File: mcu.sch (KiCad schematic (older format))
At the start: 22 parts, among them U201 STM32F072C8Tx, Y201 8MHz

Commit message: Add Fit, Manufacturer, MPN fields
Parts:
- C201, C202, R203, Y201: Fit (none) -> fit: none
- C203, C204, C205, C206, C207, C208, R201, R202, R204, W201, W202, W203, W204, W205, W206, W207, W208: Fit (none) -> fit:
- U201: Fit (none) -> fit:; MPN (none) -> STM32F072C8T6; Manufacturer (none) -> ST
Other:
- note added: "Short this footprint and power up the board to enter DFU bootloader mode."
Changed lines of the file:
@@
 F 2 "Housings_QFP:LQFP-48_7x7mm_Pitch0.5mm" H 9500 5675 50  0000 R TNN
 F 3 "" H 5800 3900 50  0000 C CNN
+F 4 "STM32F072C8T6" H 5800 3900 50  0001 C CNN "MPN"
+F 5 "ST" H 5800 3900 50  0001 C CNN "Manufacturer"
+F 6 "fit: " H 5800 3900 50  0001 C CNN "Fit"
 	1    5800 3900
 	1    0    0    -1
@@
 U 1 1 56F47B56
 P 1350 3150
-F 0 "Y201" H 1350 3250 50  0000 C CNN
-F 1 "8MHz" H 1350 3050 50  0000 C CNN
+F 0 "Y201" V 1278 3238 50  0000 L CNN
+F 1 "8MHz" V 1369 3238 50  0000 L CNN
 F 2 "Crystals:ABM3" H 1350 3150 50  0001 C CNN
 F 3 "" H 1350 3150 50  0000 C CNN
+F 4 "fit: none" V 1441 3238 25  0000 L CNN "Fit"
 	1    1350 3150
 	0    1    1    0
@@
 F 2 "Measurement_Points:Measurement_Point_Round-SMD-Pad_Small" H 9800 4700 50  0001 C CNN
 F 3 "" H 9800 4700 50  0000 C CNN
+F 4 "fit: " H 9600 4700 50  0001 C CNN "Fit"
 	1    9600 4700
 	0    1    1    0
@@
 F 2 "Measurement_Points:Measurement_Point_Round-SMD-Pad_Small" H 9800 4800 50  0001 C CNN
 F 3 "" H 9800 4800 50  0000 C CNN
+F 4 "fit: " H 9600 4800 50  0001 C CNN "Fit"
 	1    9600 4800
 	0    1    1    0
@@
 F 2 "Resistors_SMD:R_0603" V 1080 4400 50  0001 C CNN
 F 3 "" H 1150 4400 50  0000 C CNN
+F 4 "fit: " H 1150 4400 50  0001 C CNN "Fit"
 	1    1150 4400
 	0    -1   -1   0
@@
 F 2 "Resistors_SMD:R_0603" V 1080 4500 50  0001 C CNN
 F 3 "" H 1150 4500 50  0000 C CNN
+F 4 "fit: " H 1150 4500 50  0001 C CNN "Fit"
 	1    1150 4500
 	0    1    1    0
@@
 U 1 1 56F50DA3
 P 3900 6500
-F 0 "R203" V 3980 6500 50  0000 C CNN
-F 1 "R" V 3900 6500 50  0000 C CNN
+F 0 "R203" H 3970 6572 50  0000 L CNN
+F 1 "R" H 3970 6481 50  0000 L CNN
 F 2 "Resistors_SMD:R_0805" V 3830 6500 50  0001 C CNN
 F 3 "" H 3900 6500 50  0000 C CNN
+F 4 "fit: none" H 3970 6409 25  0000 L CNN "Fit"
 	1    3900 6500
 	1    0    0    -1
@@
 F 2 "Resistors_SMD:R_0603" V 3830 6900 50  0001 C CNN
 F 3 "" H 3900 6900 50  0000 C CNN
+F 4 "fit: " H 3900 6900 50  0001 C CNN "Fit"
 	1    3900 6900
 	-1   0    0    1
@@
 U 1 1 56F51A5F
 P 1100 3250
-F 0 "C202" V 950 3150 50  0000 L CNN
-F 1 "20pF" V 850 3150 50  0000 L CNN
+F 0 "C202" V 963 3250 50  0000 C CNN
+F 1 "20pF" V 872 3250 50  0000 C CNN
 F 2 "Capacitors_SMD:C_0603" H 1100 3250 50  0001 C CNN
 F 3 "" H 1100 3250 50  0000 C CNN
+F 4 "fit: none" V 800 3250 25  0000 C CNN "Fit"
 	1    1100 3250
 	0    -1   -1   0
@@
 F 2 "Capacitors_SMD:C_0603" H 2500 6850 50  0001 C CNN
 F 3 "" H 2500 6850 50  0000 C CNN
+F 4 "fit: " H 2500 6850 50  0001 C CNN "Fit"
 	1    2500 6850
 	1    0    0    -1
@@
 F 2 "Capacitors_SMD:C_0603" H 2200 6850 50  0001 C CNN
 F 3 "" H 2200 6850 50  0000 C CNN
+F 4 "fit: " H 2200 6850 50  0001 C CNN "Fit"
 	1    2200 6850
 	1    0    0    -1
@@
 F 2 "Capacitors_SMD:C_0603" H 1900 6850 50  0001 C CNN
 F 3 "" H 1900 6850 50  0000 C CNN
+F 4 "fit: " H 1900 6850 50  0001 C CNN "Fit"
 	1    1900 6850
 	1    0    0    -1
@@
 F 2 "Capacitors_SMD:C_0603" H 1600 6850 50  0001 C CNN
 F 3 "" H 1600 6850 50  0000 C CNN
+F 4 "fit: " H 1600 6850 50  0001 C CNN "Fit"
 	1    1600 6850
 	1    0    0    -1
@@
 F 2 "Capacitors_SMD:C_0805" H 2950 6850 50  0001 C CNN
 F 3 "" H 2950 6850 50  0000 C CNN
+F 4 "fit: " H 2950 6850 50  0001 C CNN "Fit"
 	1    2950 6850
 	1    0    0    -1
@@
 F 2 "Measurement_Points:Measurement_Point_Round-SMD-Pad_Small" H 1600 4400 50  0001 C CNN
 F 3 "" H 1600 4400 50  0000 C CNN
+F 4 "fit: " H 1400 4400 50  0001 C CNN "Fit"
 	1    1400 4400
 	1    0    0    -1
@@
 F 2 "Measurement_Points:Measurement_Point_Round-SMD-Pad_Small" H 1600 4500 50  0001 C CNN
 F 3 "" H 1600 4500 50  0000 C CNN
+F 4 "fit: " H 1400 4500 50  0001 C CNN "Fit"
 	1    1400 4500
 	-1   0    0    1
@@
 F 2 "Capacitors_SMD:C_0603" H 1350 2650 50  0001 C CNN
 F 3 "" H 1350 2650 50  0000 C CNN
+F 4 "fit: " H 1350 2650 50  0001 C CNN "Fit"
 	1    1350 2650
 	1    0    0    -1
@@
 F 2 "Measurement_Points:Measurement_Point_Round-SMD-Pad_Small" H 2200 5000 50  0001 C CNN
 F 3 "" H 2200 5000 50  0000 C CNN
+F 4 "fit: " H 2000 5000 50  0001 C CNN "Fit"
 	1    2000 5000
 	0    -1   -1   0
@@
 F 2 "Measurement_Points:Measurement_Point_Round-SMD-Pad_Small" H 2200 5100 50  0001 C CNN
 F 3 "" H 2200 5100 50  0000 C CNN
+F 4 "fit: " H 2000 5100 50  0001 C CNN "Fit"
 	1    2000 5100
 	0    -1   -1   0
@@
 F 2 "Measurement_Points:Measurement_Point_Round-SMD-Pad_Small" H 2200 5200 50  0001 C CNN
 F 3 "" H 2200 5200 50  0000 C CNN
+F 4 "fit: " H 2000 5200 50  0001 C CNN "Fit"
 	1    2000 5200
 	0    -1   -1   0
@@
 F 2 "Measurement_Points:Measurement_Point_Round-SMD-Pad_Small" H 2200 5300 50  0001 C CNN
 F 3 "" H 2200 5300 50  0000 C CNN
+F 4 "fit: " H 2000 5300 50  0001 C CNN "Fit"
 	1    2000 5300
 	0    -1   -1   0
@@
 U 1 1 56F518F0
 P 1100 3050
-F 0 "C201" V 1350 2950 50  0000 L CNN
-F 1 "20pF" V 1250 2950 50  0000 L CNN
+F 0 "C201" V 1381 3050 50  0000 C CNN
+F 1 "20pF" V 1290 3050 50  0000 C CNN
 F 2 "Capacitors_SMD:C_0603" H 1100 3050 50  0001 C CNN
 F 3 "" H 1100 3050 50  0000 C CNN
+F 4 "fit: none" V 1218 3050 25  0000 C CNN "Fit"
 	1    1100 3050
 	0    -1   -1   0
@@
 	900  3250 1000 3250
 Connection ~ 900  3150
+Text Notes 4250 6525 0    60   ~ 0
+Short this footprint and power up the board to enter DFU bootloader mode.
 $EndSCHEMATC

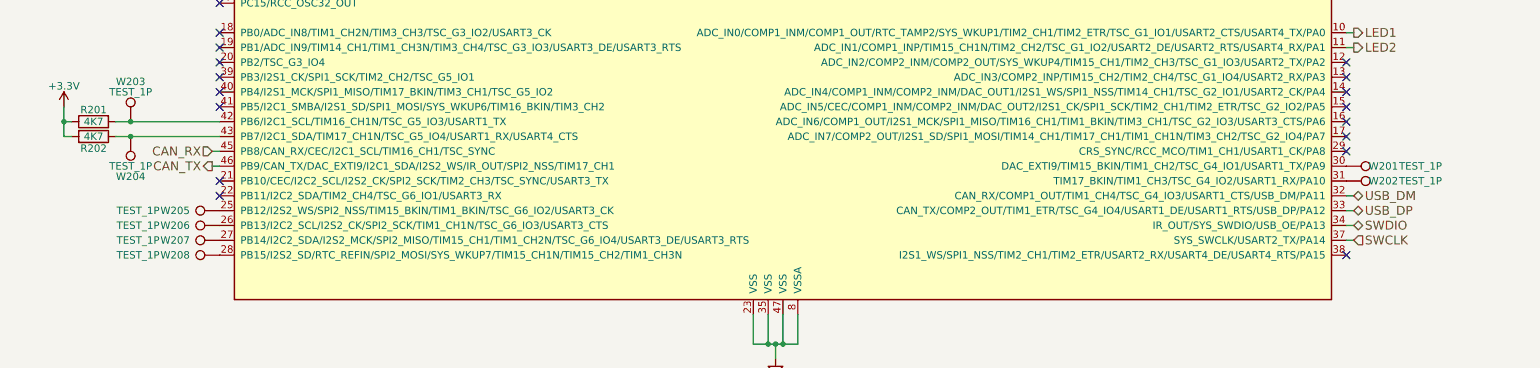
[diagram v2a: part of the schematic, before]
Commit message: Update Silkscreen and add netnames
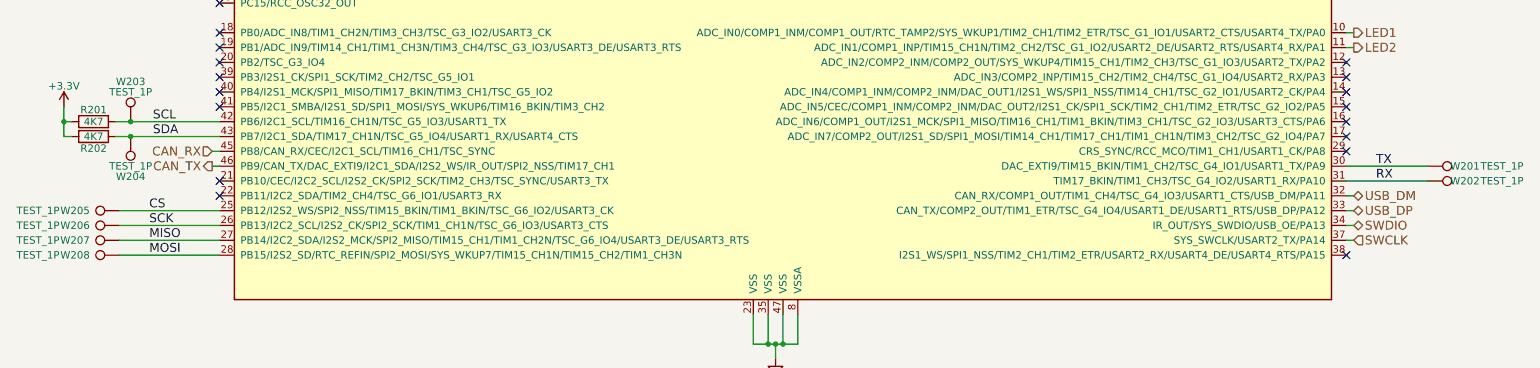
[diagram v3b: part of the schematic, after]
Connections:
- net CS: now reaches U201.25 (PB12/I2S2_WS/SPI2_NSS/TIM15_BKIN/TIM1_BKIN/TSC_G6_IO2/USART3_CK), W205.1
- net SCK: now reaches U201.26 (PB13/I2C2_SCL/I2S2_CK/SPI2_SCK/TIM1_CH1N/TSC_G6_IO3/USART3_CTS), W206.1
- net MISO: now reaches U201.27 (PB14/I2C2_SDA/I2S2_MCK/SPI2_MISO/TIM15_CH1/TIM1_CH2N/TSC_G6_IO4/USART3_DE/USART3_RTS), W207.1
- net MOSI: now reaches U201.28 (PB15/I2S2_SD/RTC_REFIN/SPI2_MOSI/SYS_WKUP7/TIM15_CH1N/TIM15_CH2/TIM1_CH3N), W208.1
- net TX: now reaches U201.30 (DAC_EXTI9/TIM15_BKIN/TIM1_CH2/TSC_G4_IO1/USART1_TX/PA9), W201.1
- net RX: now reaches U201.31 (TIM17_BKIN/TIM1_CH3/TSC_G4_IO2/USART1_RX/PA10), W202.1
- net SCL: now reaches R201.2, U201.42 (PB6/I2C1_SCL/TIM16_CH1N/TSC_G5_IO3/USART1_TX), W203.1
- net SDA: now reaches R202.1, U201.43 (PB7/I2C1_SDA/TIM17_CH1N/TSC_G5_IO4/USART1_RX/USART4_CTS), W204.1
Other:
- moved on the sheet: W201, W202, W205, W206, W207, W208
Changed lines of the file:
@@
 L candleLight-rescue:TEST_1P W201
 U 1 1 56F4FE08
-P 9600 4700
-F 0 "W201" V 9600 4950 50  0000 C CNN
-F 1 "TEST_1P" V 9600 5200 50  0000 C CNN
-F 2 "Measurement_Points:Measurement_Point_Round-SMD-Pad_Small" H 9800 4700 50  0001 C CNN
-F 3 "" H 9800 4700 50  0000 C CNN
-F 4 "fit: " H 9600 4700 50  0001 C CNN "Fit"
-	1    9600 4700
+P 10150 4700
+F 0 "W201" V 10150 4950 50  0000 C CNN
+F 1 "TEST_1P" V 10150 5200 50  0000 C CNN
+F 2 "Measurement_Points:Measurement_Point_Round-SMD-Pad_Small" H 10350 4700 50  0001 C CNN
+F 3 "" H 10350 4700 50  0000 C CNN
+F 4 "fit: " H 10150 4700 50  0001 C CNN "Fit"
+	1    10150 4700
 	0    1    1    0
 $EndComp
@@
 L candleLight-rescue:TEST_1P W202
 U 1 1 56F4FE85
-P 9600 4800
-F 0 "W202" V 9600 5050 50  0000 C CNN
-F 1 "TEST_1P" V 9600 5300 50  0000 C CNN
-F 2 "Measurement_Points:Measurement_Point_Round-SMD-Pad_Small" H 9800 4800 50  0001 C CNN
-F 3 "" H 9800 4800 50  0000 C CNN
-F 4 "fit: " H 9600 4800 50  0001 C CNN "Fit"
-	1    9600 4800
+P 10150 4800
+F 0 "W202" V 10150 5050 50  0000 C CNN
+F 1 "TEST_1P" V 10150 5300 50  0000 C CNN
+F 2 "Measurement_Points:Measurement_Point_Round-SMD-Pad_Small" H 10350 4800 50  0001 C CNN
+F 3 "" H 10350 4800 50  0000 C CNN
+F 4 "fit: " H 10150 4800 50  0001 C CNN "Fit"
+	1    10150 4800
 	0    1    1    0
 $EndComp
@@
 L candleLight-rescue:TEST_1P W205
 U 1 1 57225CE8
-P 2000 5000
-F 0 "W205" V 2000 5300 50  0000 C CNN
-F 1 "TEST_1P" V 2000 5550 50  0000 C CNN
-F 2 "Measurement_Points:Measurement_Point_Round-SMD-Pad_Small" H 2200 5000 50  0001 C CNN
-F 3 "" H 2200 5000 50  0000 C CNN
-F 4 "fit: " H 2000 5000 50  0001 C CNN "Fit"
-	1    2000 5000
+P 1325 5000
+F 0 "W205" V 1325 5300 50  0000 C CNN
+F 1 "TEST_1P" V 1325 5550 50  0000 C CNN
+F 2 "Measurement_Points:Measurement_Point_Round-SMD-Pad_Small" H 1525 5000 50  0001 C CNN
+F 3 "" H 1525 5000 50  0000 C CNN
+F 4 "fit: " H 1325 5000 50  0001 C CNN "Fit"
+	1    1325 5000
 	0    -1   -1   0
 $EndComp
@@
 L candleLight-rescue:TEST_1P W206
 U 1 1 57225F09
-P 2000 5100
-F 0 "W206" V 2000 5400 50  0000 C CNN
-F 1 "TEST_1P" V 2000 5650 50  0000 C CNN
-F 2 "Measurement_Points:Measurement_Point_Round-SMD-Pad_Small" H 2200 5100 50  0001 C CNN
-F 3 "" H 2200 5100 50  0000 C CNN
-F 4 "fit: " H 2000 5100 50  0001 C CNN "Fit"
-	1    2000 5100
+P 1325 5100
+F 0 "W206" V 1325 5400 50  0000 C CNN
+F 1 "TEST_1P" V 1325 5650 50  0000 C CNN
+F 2 "Measurement_Points:Measurement_Point_Round-SMD-Pad_Small" H 1525 5100 50  0001 C CNN
+F 3 "" H 1525 5100 50  0000 C CNN
+F 4 "fit: " H 1325 5100 50  0001 C CNN "Fit"
+	1    1325 5100
 	0    -1   -1   0
 $EndComp
@@
 L candleLight-rescue:TEST_1P W207
 U 1 1 57225F5B
-P 2000 5200
-F 0 "W207" V 2000 5500 50  0000 C CNN
-F 1 "TEST_1P" V 2000 5750 50  0000 C CNN
-F 2 "Measurement_Points:Measurement_Point_Round-SMD-Pad_Small" H 2200 5200 50  0001 C CNN
-F 3 "" H 2200 5200 50  0000 C CNN
-F 4 "fit: " H 2000 5200 50  0001 C CNN "Fit"
-	1    2000 5200
+P 1325 5200
+F 0 "W207" V 1325 5500 50  0000 C CNN
+F 1 "TEST_1P" V 1325 5750 50  0000 C CNN
+F 2 "Measurement_Points:Measurement_Point_Round-SMD-Pad_Small" H 1525 5200 50  0001 C CNN
+F 3 "" H 1525 5200 50  0000 C CNN
+F 4 "fit: " H 1325 5200 50  0001 C CNN "Fit"
+	1    1325 5200
 	0    -1   -1   0
 $EndComp
@@
 L candleLight-rescue:TEST_1P W208
 U 1 1 57225FCB
-P 2000 5300
-F 0 "W208" V 2000 5600 50  0000 C CNN
-F 1 "TEST_1P" V 2000 5850 50  0000 C CNN
-F 2 "Measurement_Points:Measurement_Point_Round-SMD-Pad_Small" H 2200 5300 50  0001 C CNN
-F 3 "" H 2200 5300 50  0000 C CNN
-F 4 "fit: " H 2000 5300 50  0001 C CNN "Fit"
-	1    2000 5300
+P 1325 5300
+F 0 "W208" V 1325 5600 50  0000 C CNN
+F 1 "TEST_1P" V 1325 5850 50  0000 C CNN
+F 2 "Measurement_Points:Measurement_Point_Round-SMD-Pad_Small" H 1525 5300 50  0001 C CNN
+F 3 "" H 1525 5300 50  0000 C CNN
+F 4 "fit: " H 1325 5300 50  0001 C CNN "Fit"
+	1    1325 5300
 	0    -1   -1   0
 $EndComp
@@
 Text Notes 4250 6525 0    60   ~ 0
 Short this footprint and power up the board to enter DFU bootloader mode.
+Wire Wire Line
+	2000 5000 1325 5000
+Wire Wire Line
+	1325 5100 2000 5100
+Wire Wire Line
+	2000 5200 1325 5200
+Wire Wire Line
+	1325 5300 2000 5300
+Wire Wire Line
+	9600 4700 10150 4700
+Wire Wire Line
+	10150 4800 9600 4800
+Text Label 9800 4700 0    60   ~ 0
+TX
+Text Label 9800 4800 0    60   ~ 0
+RX
+Text Label 1525 5000 0    60   ~ 0
+CS
+Text Label 1525 5100 0    60   ~ 0
+SCK
+Text Label 1525 5200 0    60   ~ 0
+MISO
+Text Label 1525 5300 0    60   ~ 0
+MOSI
+Text Label 1550 4400 0    60   ~ 0
+SCL
+Text Label 1550 4500 0    60   ~ 0
+SDA
 $EndSCHEMATC

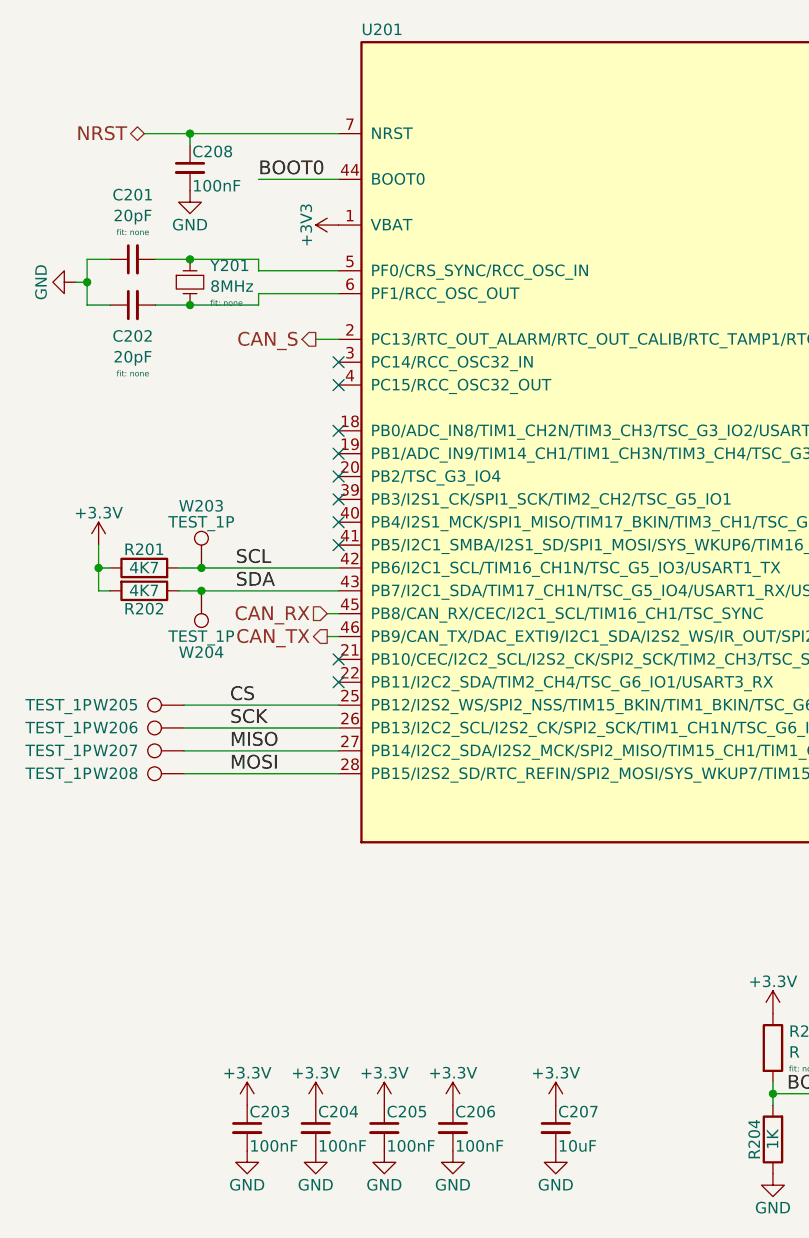
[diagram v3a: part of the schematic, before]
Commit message: Add Cap voltage rating, Put PCB ref on cupper, add note for variants
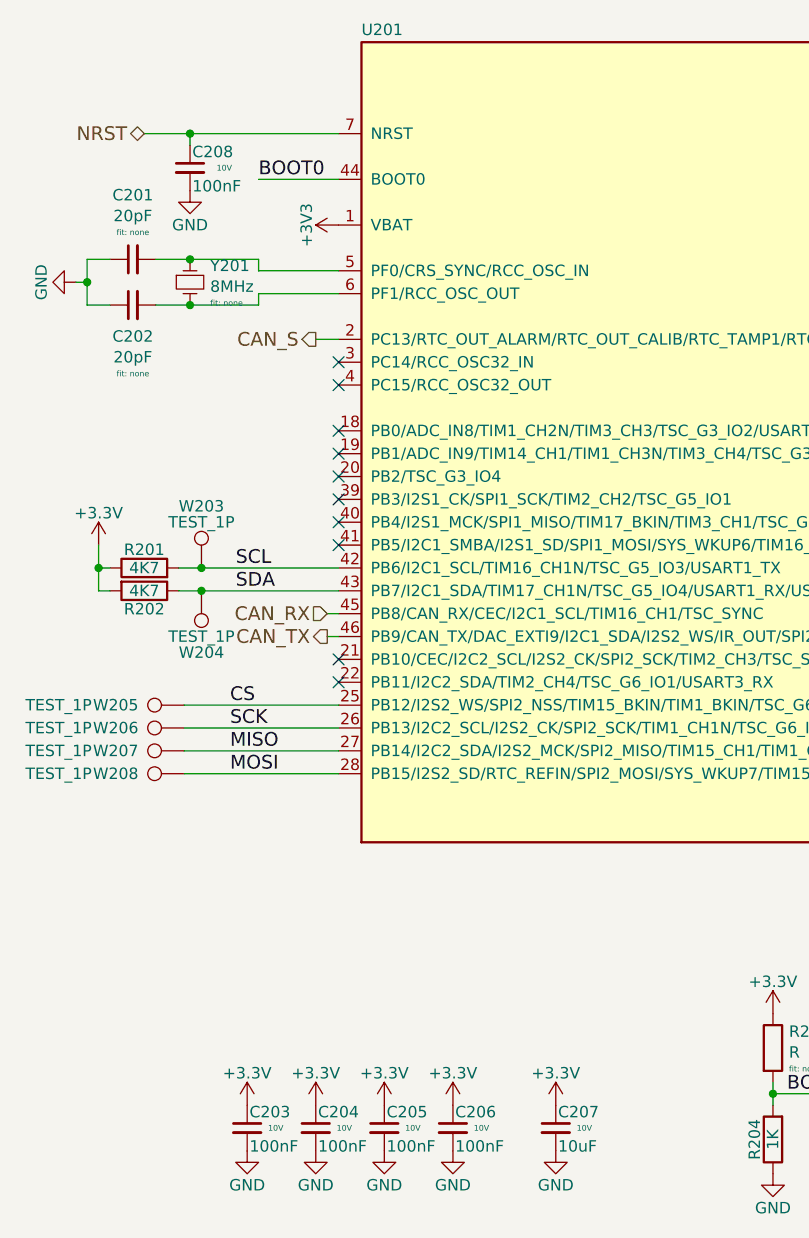
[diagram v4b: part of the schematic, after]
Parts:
- C203, C204, C205, C206, C207, C208: CapRatedVoltage (none) -> 10V
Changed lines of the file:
@@
 F 3 "" H 2500 6850 50  0000 C CNN
 F 4 "fit: " H 2500 6850 50  0001 C CNN "Fit"
+F 5 "10V" H 2625 6850 25  0000 C CNN "CapRatedVoltage"
 	1    2500 6850
 	1    0    0    -1
@@
 F 3 "" H 2200 6850 50  0000 C CNN
 F 4 "fit: " H 2200 6850 50  0001 C CNN "Fit"
+F 5 "10V" H 2325 6850 25  0000 C CNN "CapRatedVoltage"
 	1    2200 6850
 	1    0    0    -1
@@
 F 3 "" H 1900 6850 50  0000 C CNN
 F 4 "fit: " H 1900 6850 50  0001 C CNN "Fit"
+F 5 "10V" H 2025 6850 25  0000 C CNN "CapRatedVoltage"
 	1    1900 6850
 	1    0    0    -1
@@
 F 3 "" H 1600 6850 50  0000 C CNN
 F 4 "fit: " H 1600 6850 50  0001 C CNN "Fit"
+F 5 "10V" H 1725 6850 25  0000 C CNN "CapRatedVoltage"
 	1    1600 6850
 	1    0    0    -1
@@
 F 3 "" H 2950 6850 50  0000 C CNN
 F 4 "fit: " H 2950 6850 50  0001 C CNN "Fit"
+F 5 "10V" H 3075 6850 25  0000 C CNN "CapRatedVoltage"
 	1    2950 6850
 	1    0    0    -1
@@
 F 3 "" H 1350 2650 50  0000 C CNN
 F 4 "fit: " H 1350 2650 50  0001 C CNN "Fit"
+F 5 "10V" H 1500 2650 25  0000 C CNN "CapRatedVoltage"
 	1    1350 2650
 	1    0    0    -1
